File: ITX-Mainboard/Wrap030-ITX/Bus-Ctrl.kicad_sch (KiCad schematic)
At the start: 25 parts, among them J9 Conn_01x02, SW1 SW_Push, U3 74HCT04, U9 DS1813-5+T&R

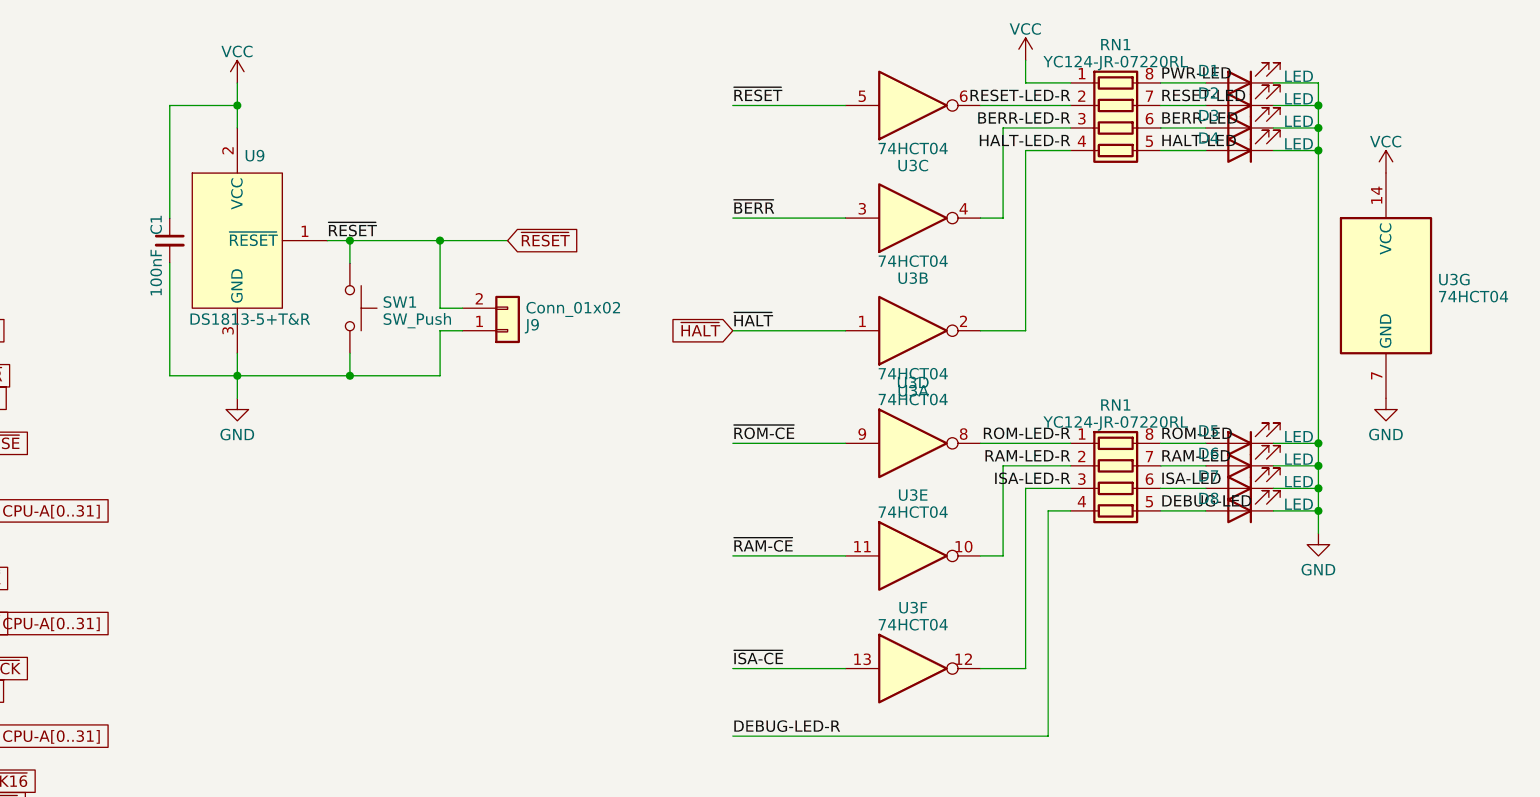
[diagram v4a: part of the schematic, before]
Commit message: PCB Silkscreen & DRC Cleanup
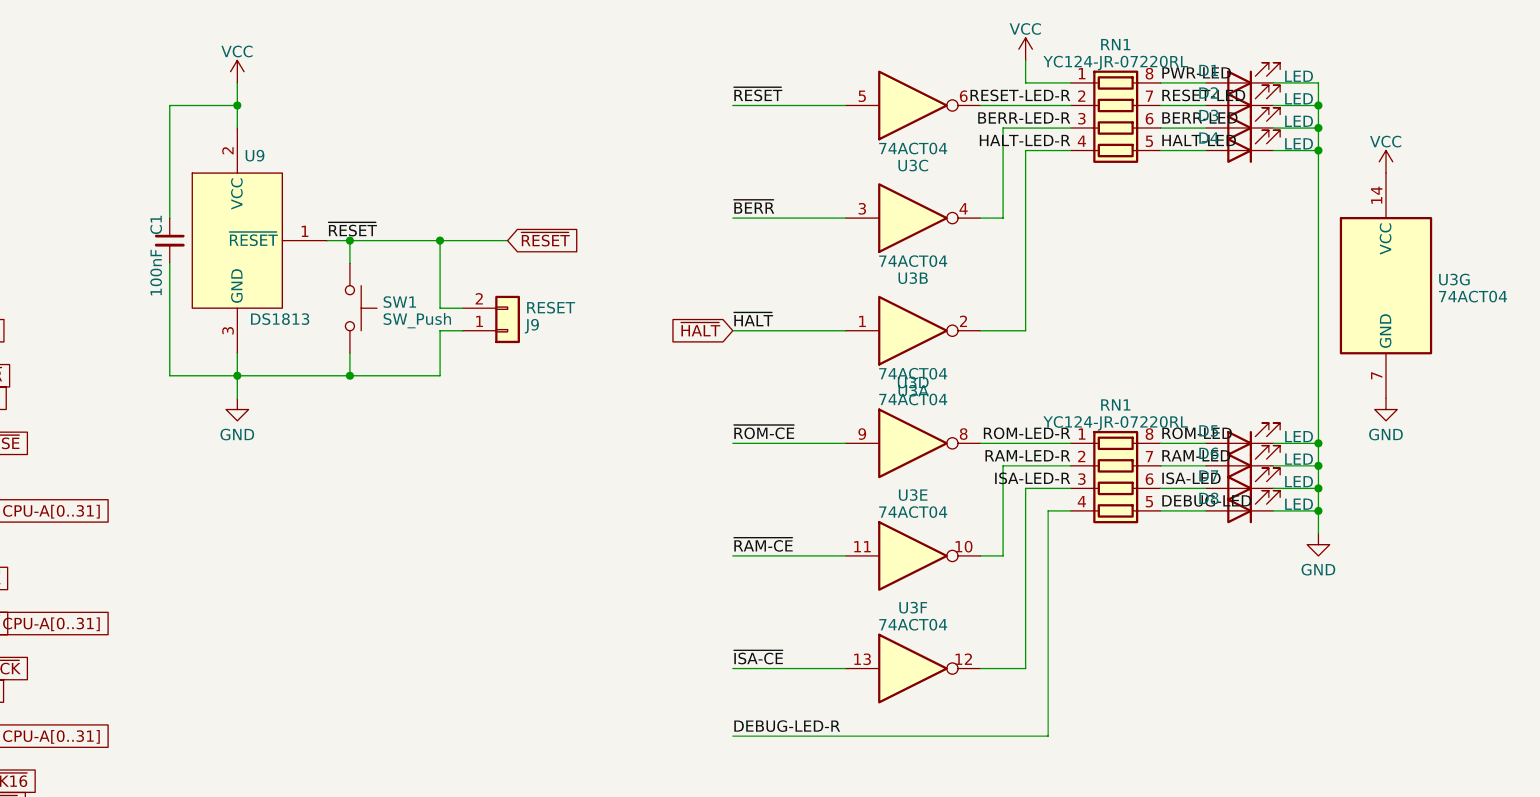
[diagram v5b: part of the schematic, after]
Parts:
- J9: value Conn_01x02 -> RESET
- U3: value 74HCT04 -> 74ACT04
- U9: value DS1813-5+T&R -> DS1813
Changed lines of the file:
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@@
       (effects (font (size 1.27 1.27)) (justify left))
     )
-    (property "Value" "74HCT04" (at 259.842 46.9973 0)
+    (property "Value" "74ACT04" (at 259.842 46.9973 0)
       (effects (font (size 1.27 1.27)) (justify left))
     )
@@
       (effects (font (size 1.27 1.27)))
     )
-    (property "Value" "74HCT04" (at 200.66 71.3011 0)
+    (property "Value" "74ACT04" (at 200.66 71.3011 0)
       (effects (font (size 1.27 1.27)))
     )
@@
       (effects (font (size 1.27 1.27)))
     )
-    (property "Value" "74HCT04" (at 200.66 42.9989 0)
+    (property "Value" "74ACT04" (at 200.66 42.9989 0)
       (effects (font (size 1.27 1.27)))
     )
@@
       (effects (font (size 1.27 1.27)))
     )
-    (property "Value" "74HCT04" (at 200.66 30.2989 0)
+    (property "Value" "74ACT04" (at 200.66 30.2989 0)
       (effects (font (size 1.27 1.27)))
     )
@@
       (effects (font (size 1.27 1.27)) (justify right))
     )
-    (property "Value" "DS1813-5+T&R" (at 132.7151 49.5373 0)
+    (property "Value" "DS1813" (at 132.7151 49.5373 0)
       (effects (font (size 1.27 1.27)) (justify right))
     )
@@
       (effects (font (size 1.27 1.27)))
     )
-    (property "Value" "74HCT04" (at 200.66 84.0011 0)
+    (property "Value" "74ACT04" (at 200.66 84.0011 0)
       (effects (font (size 1.27 1.27)))
     )
@@
       (effects (font (size 1.27 1.27)) (justify left))
     )
-    (property "Value" "Conn_01x02" (at 156.972 48.2527 0)
+    (property "Value" "RESET" (at 156.972 48.2527 0)
       (effects (font (size 1.27 1.27)) (justify left))
     )
@@
       (effects (font (size 1.27 1.27)))
     )
-    (property "Value" "74HCT04" (at 200.66 55.6989 0)
+    (property "Value" "74ACT04" (at 200.66 55.6989 0)
       (effects (font (size 1.27 1.27)))
     )
@@
       (effects (font (size 1.27 1.27)))
     )
-    (property "Value" "74HCT04" (at 200.66 58.6011 0)
-      (effects (font (size 1.27 1.27)))
-    )
+    (property "Value" "74ACT04" (at 200.66 58.6011 0)
+      (effects (font (size 1.27 1.27)))
+    )

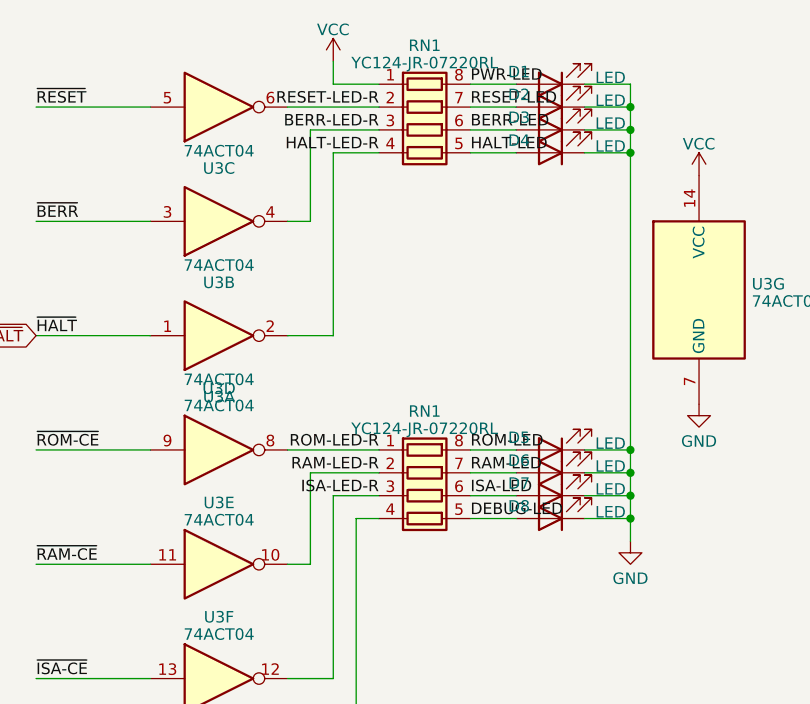
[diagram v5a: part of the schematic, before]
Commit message: Replace resistor nets with 0402 & update gerbers
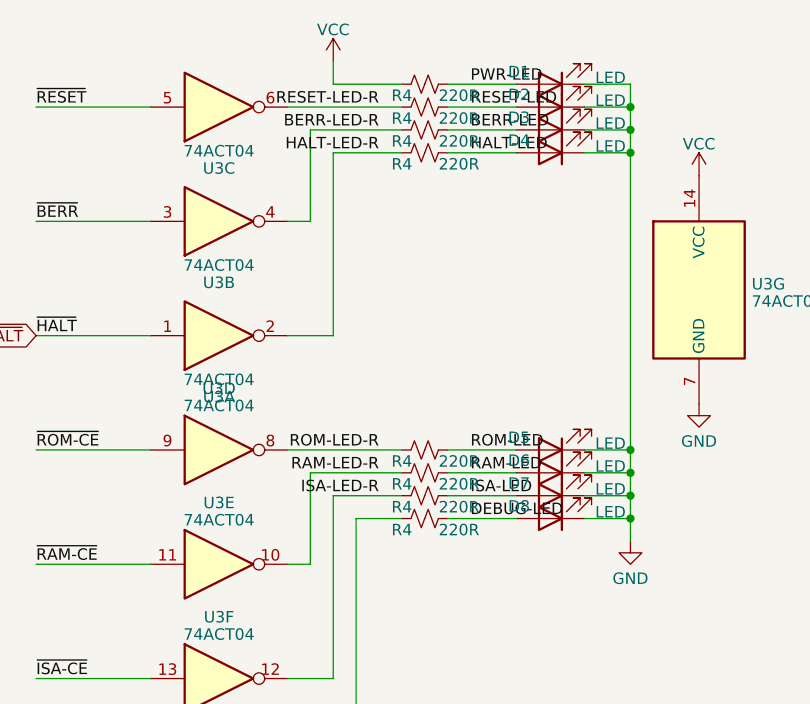
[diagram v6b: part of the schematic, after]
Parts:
- removed RN1 (x2): YC124-JR-07220RL, Resistor_SMD:R_Array_Convex_4x1206, symbol Device:R_Pack04
- added R4 (x8): 220R, Resistor_SMD:R_0402_1005Metric_Pad0.72x0.64mm_HandSolder, symbol Device:R_Small_US
- C1: Mouser-Part (none) -> 187-CL05B104KO5NNNC; Notes (none) -> JLC
- C15: Mouser-Part (none) -> 187-CL05A105KA5NQNC; Notes (none) -> JLC
- D1, D2, D3, D4, D5, D6, D7, D8: Mouser-Part (none) -> 859-LTL1CHJETNN; Notes (none) -> OFE
- J9: Mouser-Part (none) -> 523-G800NA306018EU; Notes (none) -> OFE
- SW1: Mouser-Part (none) -> 179-TS026660BK260LCR; Notes (none) -> OFE
- U3: Mouser-Part (none) -> 595-SN74ACT04N; Notes (none) -> OFE; Socket-Mouser (none) -> 571-1-2199298-3
- U9: Notes (none) -> OFE
- VGEN1: Mouser-Part (none) -> 556-ATF1508AS-10JU84; Notes (none) -> OFE; Socket-Mouser (none) -> 575-948424
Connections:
- net BERR-LED: now also R4.2
- net BERR-LED-R: now also R4.1
- net DEBUG-LED: now also R4.2
- net DEBUG-LED-R: now also R4.1
- net HALT-LED: now also R4.2
- net HALT-LED-R: now also R4.1
- net ISA-LED: now also R4.2
- net ISA-LED-R: now also R4.1
- net PWR-LED: now also R4.2
- net RAM-LED: now also R4.2
- net RAM-LED-R: now also R4.1
- net RESET-LED: now also R4.2
- net RESET-LED-R: now also R4.1
- net ROM-LED: now also R4.2
- net ROM-LED-R: now also R4.1
- net VCC: now also R4.1
